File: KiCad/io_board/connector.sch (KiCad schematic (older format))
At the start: 2 parts

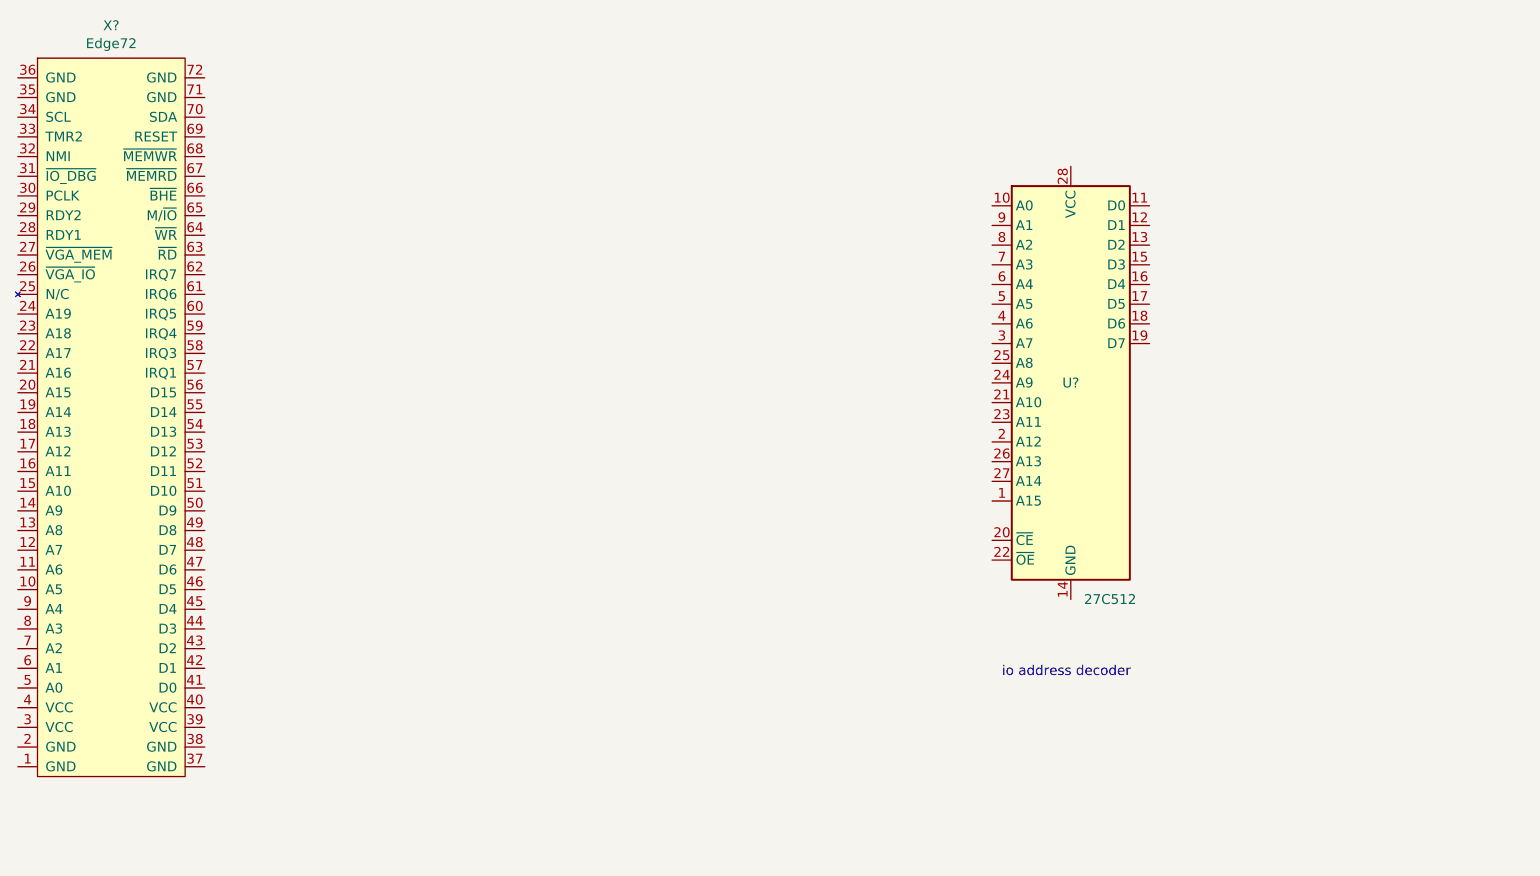
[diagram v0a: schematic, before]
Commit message: Updated IO board schematics and board.
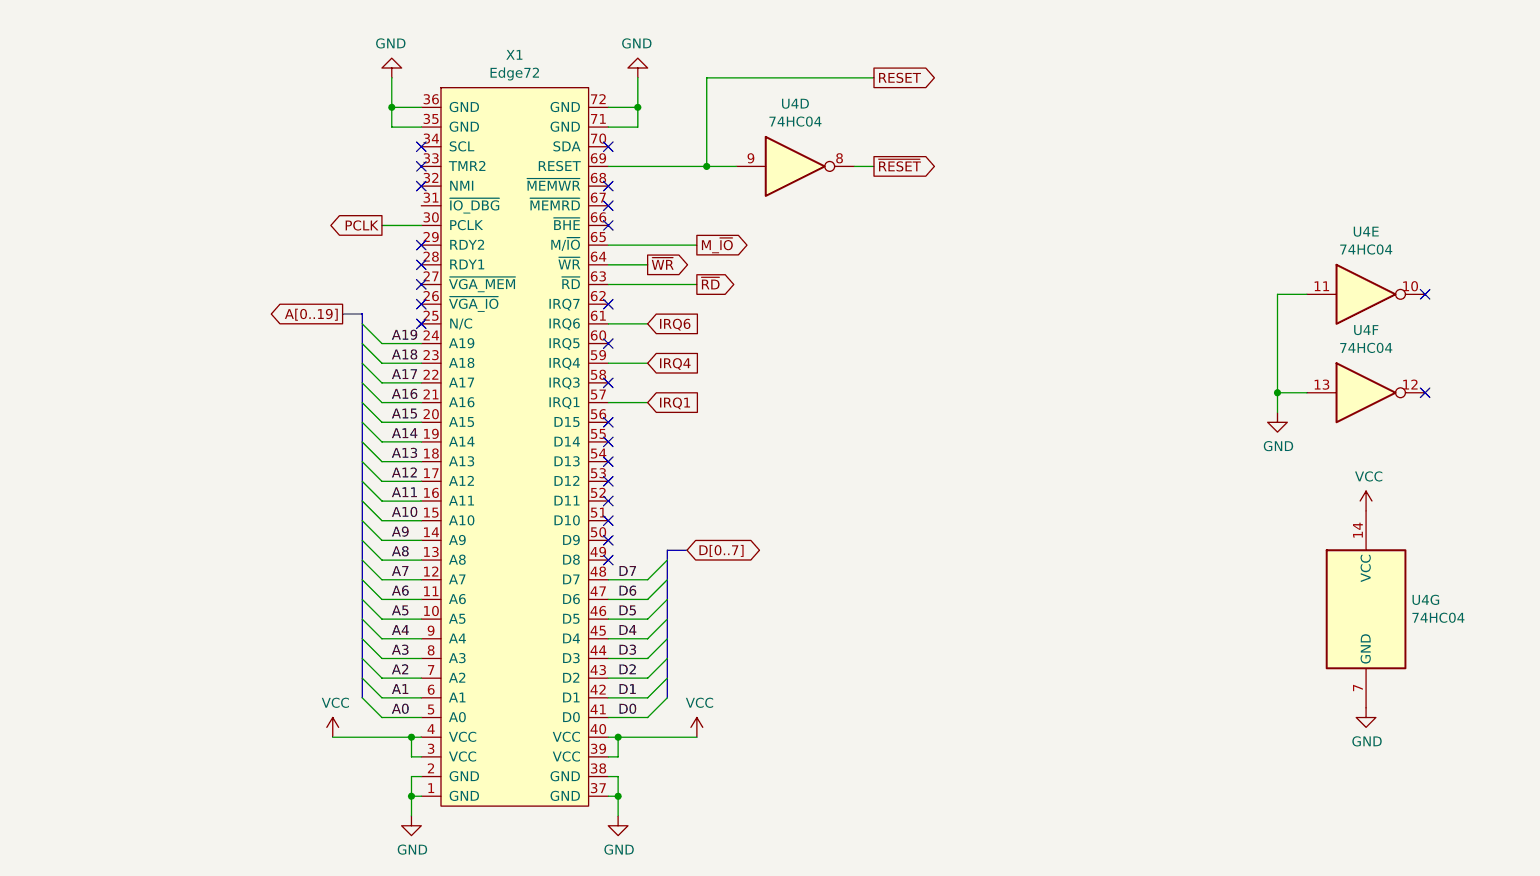
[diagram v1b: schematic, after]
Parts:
- removed U?: 27C512, Package_DIP:DIP-28_W15.24mm, symbol Memory_EPROM:27C512
- added U4: 74HC04, symbol 74xx:74HC04
- X1: renamed from X?; footprint (none) -> Mini8086:BUS_72
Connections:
- net GND: now reaches X1.1 (GND)
- net GND: now also X1.2 (GND), X1.35 (GND), X1.36 (GND), X1.37 (GND), X1.38 (GND), X1.71 (GND), X1.72 (GND), U4.11, U4.13, U4.7 (GND)
- net A5: now reaches X1.10 (A5)
- net A6: now reaches X1.11 (A6)
- net A7: now reaches X1.12 (A7)
- net A8: now reaches X1.13 (A8)
- net A9: now reaches X1.14 (A9)
- net A10: now reaches X1.15 (A10)
- net A11: now reaches X1.16 (A11)
- net A12: now reaches X1.17 (A12)
- net A13: now reaches X1.18 (A13)
- net A14: now reaches X1.19 (A14)
- net A15: now reaches X1.20 (A15)
- net A16: now reaches X1.21 (A16)
- net A17: now reaches X1.22 (A17)
- net A18: now reaches X1.23 (A18)
- net A19: now reaches X1.24 (A19)
- net VCC: now reaches X1.3 (VCC)
- net VCC: now also X1.39 (VCC), X1.4 (VCC), X1.40 (VCC), U4.14 (VCC)
- net PCLK: now reaches X1.30 (PCLK)
- net D0: now reaches X1.41 (D0)
- net D1: now reaches X1.42 (D1)
- net D2: now reaches X1.43 (D2)
- net D3: now reaches X1.44 (D3)
- net D4: now reaches X1.45 (D4)
- net D5: now reaches X1.46 (D5)
- net D6: now reaches X1.47 (D6)
- net D7: now reaches X1.48 (D7)
- net A0: now reaches X1.5 (A0)
- net IRQ1: now reaches X1.57 (IRQ1)
- net IRQ4: now reaches X1.59 (IRQ4)
- net A1: now reaches X1.6 (A1)
- net IRQ6: now reaches X1.61 (IRQ6)
- net ~RD: now reaches X1.63 (~RD)
- net ~WR: now reaches X1.64 (~WR)
- net M_~IO: now reaches X1.65 (M/~IO)
- net RESET: now reaches X1.69 (RESET)
- net RESET: now also U4.9
- net A2: now reaches X1.7 (A2)
- net A3: now reaches X1.8 (A3)
- net A4: now reaches X1.9 (A4)
- new net ~RESET: U4.8
- no-connect marks 0 -> 25
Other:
- note removed: "io address decoder"
- moved on the sheet: X1

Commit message: Worked on I/O board.
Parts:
- U4: footprint (none) -> Package_SO:SOIC-14_3.9x8.7mm_P1.27mm
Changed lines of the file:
@@
 $Descr A4 11693 8268
 encoding utf-8
-Sheet 5 7
-Title ""
-Date ""
+Sheet 6 7
+Title "Mini8086 I/O board"
+Date "2020-11-05"
 Rev "1.0"
 Comp ""
@@
 F 0 "U4" H 5450 2217 50  0000 C CNN
 F 1 "74HC04" H 5450 2126 50  0000 C CNN
-F 2 "" H 5450 1900 50  0001 C CNN
+F 2 "Package_SO:SOIC-14_3.9x8.7mm_P1.27mm" H 5450 1900 50  0001 C CNN
 F 3 "https://assets.nexperia.com/documents/data-sheet/74HC_HCT04.pdf" H 5450 1900 50  0001 C CNN
 	4    5450 1900
@@
 F 0 "U4" H 8350 2867 50  0000 C CNN
 F 1 "74HC04" H 8350 2776 50  0000 C CNN
-F 2 "" H 8350 2550 50  0001 C CNN
+F 2 "Package_SO:SOIC-14_3.9x8.7mm_P1.27mm" H 8350 2550 50  0001 C CNN
 F 3 "https://assets.nexperia.com/documents/data-sheet/74HC_HCT04.pdf" H 8350 2550 50  0001 C CNN
 	5    8350 2550
@@
 F 0 "U4" H 8350 3367 50  0000 C CNN
 F 1 "74HC04" H 8350 3276 50  0000 C CNN
-F 2 "" H 8350 3050 50  0001 C CNN
+F 2 "Package_SO:SOIC-14_3.9x8.7mm_P1.27mm" H 8350 3050 50  0001 C CNN
 F 3 "https://assets.nexperia.com/documents/data-sheet/74HC_HCT04.pdf" H 8350 3050 50  0001 C CNN
 	6    8350 3050
@@
 F 0 "U4" H 8580 4196 50  0000 L CNN
 F 1 "74HC04" H 8580 4105 50  0000 L CNN
-F 2 "" H 8350 4150 50  0001 C CNN
+F 2 "Package_SO:SOIC-14_3.9x8.7mm_P1.27mm" H 8350 4150 50  0001 C CNN
 F 3 "https://assets.nexperia.com/documents/data-sheet/74HC_HCT04.pdf" H 8350 4150 50  0001 C CNN
 	7    8350 4150

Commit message: Working on IO board
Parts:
- U4: value 74HC04 -> 74HCT04
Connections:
- net GND: no longer U4.11
- net IRQ7: now reaches X1.62 (IRQ7)
- net IRQ7: now also U4.10
- new net ~INT_I2C: U4.11
- no-connect marks 25 -> 23
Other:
- moved on the sheet: U4E
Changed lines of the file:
@@
 $Descr A4 11693 8268
 encoding utf-8
-Sheet 6 7
+Sheet 6 8
 Title "Mini8086 I/O board"
 Date "2020-11-05"
@@
 NoConn ~ 4500 3000
 NoConn ~ 4500 2800
-NoConn ~ 4500 2600
 Wire Wire Line
 	3550 2200 3350 2200
@@
 P 5450 1900
 F 0 "U4" H 5450 2217 50  0000 C CNN
-F 1 "74HC04" H 5450 2126 50  0000 C CNN
+F 1 "74HCT04" H 5450 2126 50  0000 C CNN
 F 2 "Package_SO:SOIC-14_3.9x8.7mm_P1.27mm" H 5450 1900 50  0001 C CNN
 F 3 "https://assets.nexperia.com/documents/data-sheet/74HC_HCT04.pdf" H 5450 1900 50  0001 C CNN
@@
 L 74xx:74HC04 U4
 U 5 1 5F90312F
-P 8350 2550
-F 0 "U4" H 8350 2867 50  0000 C CNN
-F 1 "74HC04" H 8350 2776 50  0000 C CNN
-F 2 "Package_SO:SOIC-14_3.9x8.7mm_P1.27mm" H 8350 2550 50  0001 C CNN
-F 3 "https://assets.nexperia.com/documents/data-sheet/74HC_HCT04.pdf" H 8350 2550 50  0001 C CNN
-	5    8350 2550
-	1    0    0    -1
+P 5450 2600
+F 0 "U4" H 5450 2917 50  0000 C CNN
+F 1 "74HCT04" H 5450 2826 50  0000 C CNN
+F 2 "Package_SO:SOIC-14_3.9x8.7mm_P1.27mm" H 5450 2600 50  0001 C CNN
+F 3 "https://assets.nexperia.com/documents/data-sheet/74HC_HCT04.pdf" H 5450 2600 50  0001 C CNN
+	5    5450 2600
+	-1   0    0    1
 $EndComp
 $Comp
@@
 P 8350 3050
 F 0 "U4" H 8350 3367 50  0000 C CNN
-F 1 "74HC04" H 8350 3276 50  0000 C CNN
+F 1 "74HCT04" H 8350 3276 50  0000 C CNN
 F 2 "Package_SO:SOIC-14_3.9x8.7mm_P1.27mm" H 8350 3050 50  0001 C CNN
 F 3 "https://assets.nexperia.com/documents/data-sheet/74HC_HCT04.pdf" H 8350 3050 50  0001 C CNN
@@
 P 8350 4150
 F 0 "U4" H 8580 4196 50  0000 L CNN
-F 1 "74HC04" H 8580 4105 50  0000 L CNN
+F 1 "74HCT04" H 8580 4105 50  0000 L CNN
 F 2 "Package_SO:SOIC-14_3.9x8.7mm_P1.27mm" H 8350 4150 50  0001 C CNN
 F 3 "https://assets.nexperia.com/documents/data-sheet/74HC_HCT04.pdf" H 8350 4150 50  0001 C CNN
@@
 	8050 3050 7900 3050
 Wire Wire Line
-	7900 3050 7900 2550
-Wire Wire Line
-	7900 2550 8050 2550
-Wire Wire Line
 	7900 3050 7900 3150
-Connection ~ 7900 3050
 $Comp
 L power:GND #PWR057
@@
 $EndComp
 NoConn ~ 8650 3050
-NoConn ~ 8650 2550
+Wire Wire Line
+	5150 2600 4500 2600
+Wire Wire Line
+	5750 2600 5850 2600
+Text GLabel 5850 2600 2    50   Input ~ 0
+~INT_I2C
+Text Label 4700 2600 0    50   ~ 0
+IRQ7
 Wire Bus Line
 	4800 3850 4800 4600

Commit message: Worked on I/O board.
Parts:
- X1: symbol Mini8086:Edge72 -> io_board-rescue:Edge72-Mini8086
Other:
- moved on the sheet: U4F, U4G
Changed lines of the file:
@@
 $EndDescr
 $Comp
-L Mini8086:Edge72 X1
+L io_board-rescue:Edge72-Mini8086 X1
 U 1 1 5F806705
 P 4000 3300
+AR Path="/5F806705" Ref="X1"  Part="1"
+AR Path="/5F8065B9/5F806705" Ref="X1"  Part="1"
 F 0 "X1" H 4025 5265 50  0000 C CNN
 F 1 "Edge72" H 4025 5174 50  0000 C CNN
@@
 L 74xx:74HC04 U4
 U 6 1 5F904907
-P 8350 3050
-F 0 "U4" H 8350 3367 50  0000 C CNN
-F 1 "74HCT04" H 8350 3276 50  0000 C CNN
-F 2 "Package_SO:SOIC-14_3.9x8.7mm_P1.27mm" H 8350 3050 50  0001 C CNN
-F 3 "https://assets.nexperia.com/documents/data-sheet/74HC_HCT04.pdf" H 8350 3050 50  0001 C CNN
-	6    8350 3050
+P 8550 2950
+F 0 "U4" H 8550 3267 50  0000 C CNN
+F 1 "74HCT04" H 8550 3176 50  0000 C CNN
+F 2 "Package_SO:SOIC-14_3.9x8.7mm_P1.27mm" H 8550 2950 50  0001 C CNN
+F 3 "https://assets.nexperia.com/documents/data-sheet/74HC_HCT04.pdf" H 8550 2950 50  0001 C CNN
+	6    8550 2950
 	1    0    0    -1
 $EndComp
@@
 L 74xx:74HC04 U4
 U 7 1 5F904FC3
-P 8350 4150
-F 0 "U4" H 8580 4196 50  0000 L CNN
-F 1 "74HCT04" H 8580 4105 50  0000 L CNN
-F 2 "Package_SO:SOIC-14_3.9x8.7mm_P1.27mm" H 8350 4150 50  0001 C CNN
-F 3 "https://assets.nexperia.com/documents/data-sheet/74HC_HCT04.pdf" H 8350 4150 50  0001 C CNN
-	7    8350 4150
+P 8550 4050
+F 0 "U4" H 8780 4096 50  0000 L CNN
+F 1 "74HCT04" H 8780 4005 50  0000 L CNN
+F 2 "Package_SO:SOIC-14_3.9x8.7mm_P1.27mm" H 8550 4050 50  0001 C CNN
+F 3 "https://assets.nexperia.com/documents/data-sheet/74HC_HCT04.pdf" H 8550 4050 50  0001 C CNN
+	7    8550 4050
 	1    0    0    -1
 $EndComp
@@
 L power:GND #PWR059
 U 1 1 5F90625F
-P 8350 4650
-F 0 "#PWR059" H 8350 4400 50  0001 C CNN
-F 1 "GND" H 8355 4477 50  0000 C CNN
-F 2 "" H 8350 4650 50  0001 C CNN
-F 3 "" H 8350 4650 50  0001 C CNN
-	1    8350 4650
+P 8550 4550
+F 0 "#PWR059" H 8550 4300 50  0001 C CNN
+F 1 "GND" H 8555 4377 50  0000 C CNN
+F 2 "" H 8550 4550 50  0001 C CNN
+F 3 "" H 8550 4550 50  0001 C CNN
+	1    8550 4550
 	1    0    0    -1
 $EndComp
@@
 L power:VCC #PWR058
 U 1 1 5F90653C
-P 8350 3650
-F 0 "#PWR058" H 8350 3500 50  0001 C CNN
-F 1 "VCC" H 8365 3823 50  0000 C CNN
-F 2 "" H 8350 3650 50  0001 C CNN
-F 3 "" H 8350 3650 50  0001 C CNN
-	1    8350 3650
-	1    0    0    -1
-$EndComp
-Wire Wire Line
-	8050 3050 7900 3050
-Wire Wire Line
-	7900 3050 7900 3150
+P 8550 3550
+F 0 "#PWR058" H 8550 3400 50  0001 C CNN
+F 1 "VCC" H 8565 3723 50  0000 C CNN
+F 2 "" H 8550 3550 50  0001 C CNN
+F 3 "" H 8550 3550 50  0001 C CNN
+	1    8550 3550
+	1    0    0    -1
+$EndComp
+Wire Wire Line
+	8250 2950 8100 2950
+Wire Wire Line
+	8100 2950 8100 3050
 $Comp
 L power:GND #PWR057
 U 1 1 5F90A6C0
-P 7900 3150
-F 0 "#PWR057" H 7900 2900 50  0001 C CNN
-F 1 "GND" H 7905 2977 50  0000 C CNN
-F 2 "" H 7900 3150 50  0001 C CNN
-F 3 "" H 7900 3150 50  0001 C CNN
-	1    7900 3150
-	1    0    0    -1
-$EndComp
-NoConn ~ 8650 3050
+P 8100 3050
+F 0 "#PWR057" H 8100 2800 50  0001 C CNN
+F 1 "GND" H 8105 2877 50  0000 C CNN
+F 2 "" H 8100 3050 50  0001 C CNN
+F 3 "" H 8100 3050 50  0001 C CNN
+	1    8100 3050
+	1    0    0    -1
+$EndComp
+NoConn ~ 8850 2950
 Wire Wire Line
 	5150 2600 4500 2600

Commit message: Worked on I/O board.
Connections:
- net A11: no longer names the net of X1.16 (A11)
- net A12: no longer names the net of X1.17 (A12)
- net A13: no longer names the net of X1.18 (A13)
- net A14: no longer names the net of X1.19 (A14)
- net A15: no longer names the net of X1.20 (A15)
- net A16: no longer names the net of X1.21 (A16)
- net A17: no longer names the net of X1.22 (A17)
- net A18: no longer names the net of X1.23 (A18)
- net A19: no longer names the net of X1.24 (A19)
- no-connect marks 23 -> 33
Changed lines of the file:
@@
 Wire Wire Line
 	3350 3800 3550 3800
-Wire Wire Line
-	3350 3700 3550 3700
-Wire Wire Line
-	3350 3600 3550 3600
-Wire Wire Line
-	3350 3500 3550 3500
-Wire Wire Line
-	3350 3400 3550 3400
-Wire Wire Line
-	3350 3300 3550 3300
-Wire Wire Line
-	3550 3200 3350 3200
-Wire Wire Line
-	3350 3100 3550 3100
-Wire Wire Line
-	3350 3000 3550 3000
-Wire Wire Line
-	3350 2900 3550 2900
-Wire Wire Line
-	3350 2800 3550 2800
-Entry Wire Line
-	3350 2800 3250 2700
-Entry Wire Line
-	3350 2900 3250 2800
-Entry Wire Line
-	3350 3000 3250 2900
-Entry Wire Line
-	3350 3100 3250 3000
-Entry Wire Line
-	3350 3200 3250 3100
-Entry Wire Line
-	3350 3300 3250 3200
-Entry Wire Line
-	3350 3400 3250 3300
-Entry Wire Line
-	3350 3500 3250 3400
-Entry Wire Line
-	3350 3600 3250 3500
 Entry Wire Line
 	3350 3700 3250 3600
@@
 	3350 4700 3250 4600
 Wire Bus Line
-	3250 2650 3150 2650
-Text GLabel 3150 2650 0    50   Output ~ 0
+	3250 3500 3150 3500
+Text GLabel 3150 3500 0    50   Output ~ 0
 A[0..19]
 NoConn ~ 3550 2600
@@
 Text Label 3400 3800 0    50   ~ 0
 A9
-Text Label 3400 3700 0    50   ~ 0
-A10
-Text Label 3400 3600 0    50   ~ 0
-A11
-Text Label 3400 3500 0    50   ~ 0
-A12
-Text Label 3400 3400 0    50   ~ 0
-A13
-Text Label 3400 3300 0    50   ~ 0
-A14
-Text Label 3400 3200 0    50   ~ 0
-A15
-Text Label 3400 3100 0    50   ~ 0
-A16
-Text Label 3400 3000 0    50   ~ 0
-A17
-Text Label 3400 2900 0    50   ~ 0
-A18
-Text Label 3400 2800 0    50   ~ 0
-A19
 NoConn ~ 3550 2700
 NoConn ~ 3550 2300
@@
 Text Label 4700 2600 0    50   ~ 0
 IRQ7
+NoConn ~ 3550 2100
+NoConn ~ 3550 3600
+NoConn ~ 3550 3500
+NoConn ~ 3550 3400
+NoConn ~ 3550 3300
+NoConn ~ 3550 2800
+NoConn ~ 3550 3200
+NoConn ~ 3550 3100
+NoConn ~ 3550 3000
+NoConn ~ 3550 2900
+Wire Wire Line
+	3550 3700 3350 3700
 Wire Bus Line
 	4800 3850 4800 4600
 Wire Bus Line
-	3250 2650 3250 4600
+	3250 3500 3250 4600
+Text Label 3400 3700 0    50   ~ 0
+A10
 $EndSCHEMATC

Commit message: Updated I/O board
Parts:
- removed X1: Edge72, Mini8086:BUS_72, symbol io_board-rescue:Edge72-Mini8086
- added X1: Edge72, Mini8086:BUS_72, symbol Mini8086:Edge72
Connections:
- net A0: now also X1.5 (A0)
- net A1: now also X1.6 (A1)
- net A10: now also X1.15 (A10)
- net A2: now also X1.7 (A2)
- net A3: now also X1.8 (A3)
- net A4: now also X1.9 (A4)
- net A5: now also X1.10 (A5)
- net A6: now also X1.11 (A6)
- net A7: now also X1.12 (A7)
- net A8: now also X1.13 (A8)
- net A9: now also X1.14 (A9)
- net D0: now also X1.41 (D0)
- net D1: now also X1.42 (D1)
- net D2: now also X1.43 (D2)
- net D3: now also X1.44 (D3)
- net D4: now also X1.45 (D4)
- net D5: now also X1.46 (D5)
- net D6: now also X1.47 (D6)
- net D7: now also X1.48 (D7)
- net GND: now also X1.1 (GND), X1.2 (GND), X1.35 (GND), X1.36 (GND), X1.37 (GND), X1.38 (GND), X1.71 (GND), X1.72 (GND)
- net IRQ1: now also X1.57 (IRQ1)
- net IRQ4: now also X1.59 (IRQ4)
- net IRQ6: now also X1.61 (IRQ6)
- net IRQ7: now also X1.62 (IRQ7)
- net M_~IO: now also X1.65 (M/~IO)
- net PCLK: now also X1.30 (PCLK)
- net RESET: now also X1.69 (RESET)
- net VCC: now also X1.3 (VCC), X1.39 (VCC), X1.4 (VCC), X1.40 (VCC)
- net ~RD: now also X1.63 (~RD)
- net ~WR: now also X1.64 (~WR)
- new net SCL: X1.34 (SCL)
- new net SDA: X1.70 (SDA)
- no-connect marks 33 -> 31
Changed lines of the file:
@@
 Comment4 ""
 $EndDescr
-$Comp
-L io_board-rescue:Edge72-Mini8086 X1
-U 1 1 5F806705
-P 4000 3300
-AR Path="/5F806705" Ref="X1"  Part="1"
-AR Path="/5F8065B9/5F806705" Ref="X1"  Part="1"
-F 0 "X1" H 4025 5265 50  0000 C CNN
-F 1 "Edge72" H 4025 5174 50  0000 C CNN
-F 2 "Mini8086:BUS_72" H 4550 3300 50  0001 C CNN
-F 3 "" H 4550 3300 50  0001 C CNN
-	1    4000 3300
-	1    0    0    -1
-$EndComp
 NoConn ~ 4500 3200
 NoConn ~ 4500 3300
@@
 NoConn ~ 3550 1900
 NoConn ~ 3550 2000
-NoConn ~ 3550 1800
-NoConn ~ 4500 1800
 Text GLabel 5850 1450 2    50   Output ~ 0
 RESET
@@
 Wire Wire Line
 	3550 3700 3350 3700
+Text Label 3400 3700 0    50   ~ 0
+A10
+$Comp
+L Mini8086:Edge72 X1
+U 1 1 60029863
+P 4000 3300
+F 0 "X1" H 4025 5265 50  0000 C CNN
+F 1 "Edge72" H 4025 5174 50  0000 C CNN
+F 2 "Mini8086:BUS_72" H 4550 3300 50  0001 C CNN
+F 3 "" H 4550 3300 50  0001 C CNN
+	1    4000 3300
+	1    0    0    -1
+$EndComp
+Wire Wire Line
+	3350 1800 3550 1800
+Wire Wire Line
+	4500 1800 4700 1800
 Wire Bus Line
 	4800 3850 4800 4600
 Wire Bus Line
 	3250 3500 3250 4600
-Text Label 3400 3700 0    50   ~ 0
-A10
+Text GLabel 3350 1800 0    50   Input ~ 0
+SCL
+Text GLabel 4700 1800 2    50   Input ~ 0
+SDA
 $EndSCHEMATC
